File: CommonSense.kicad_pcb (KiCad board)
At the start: 2 copper layers, 34 x 24 mm, 31 parts, among them J1 Conn_02x04_Counter_Clockwise, U1 NRF52810-QFAA-R7, U2 SHT41-AD1B-R2, Y1 ECS-.327-12.5-12R-TR, Y2 ABM11W-32.0000MHZ-7-D1X-T3

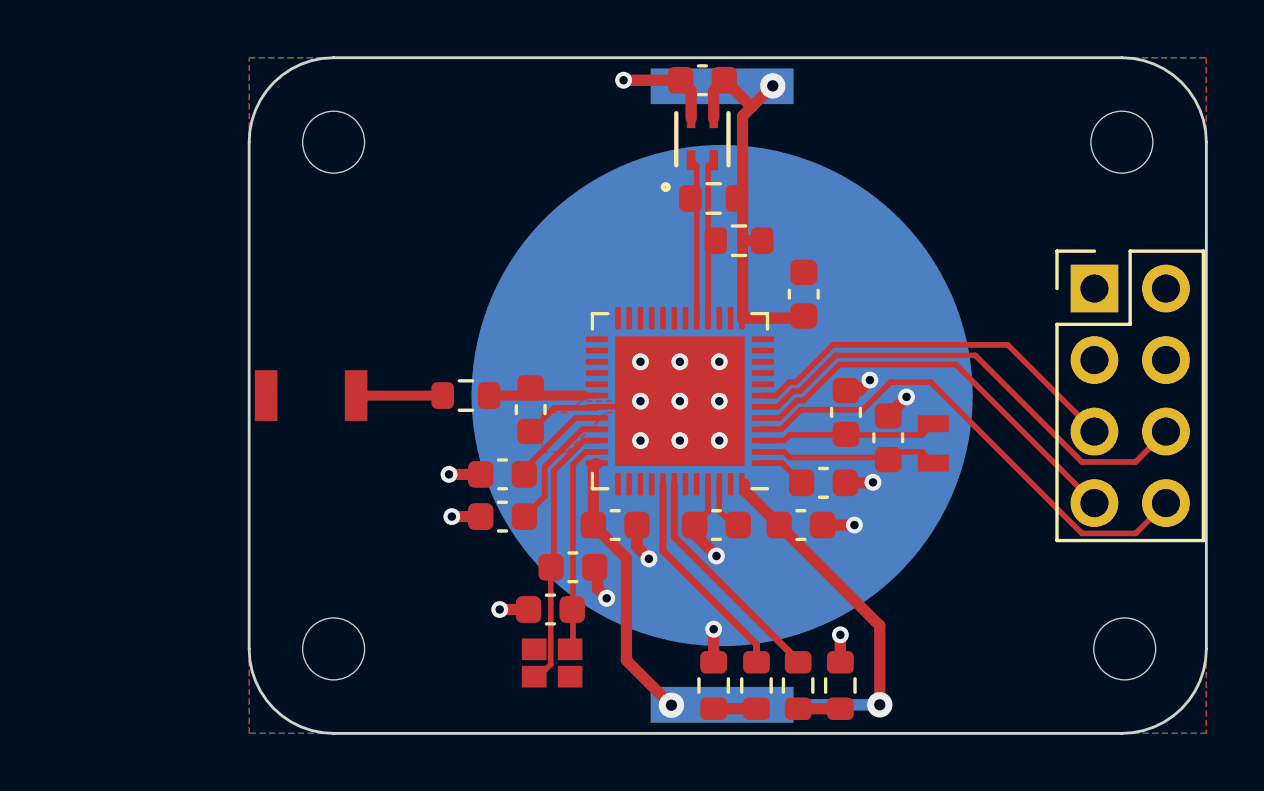
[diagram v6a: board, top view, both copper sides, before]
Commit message: Finish routing ADC in IO pins
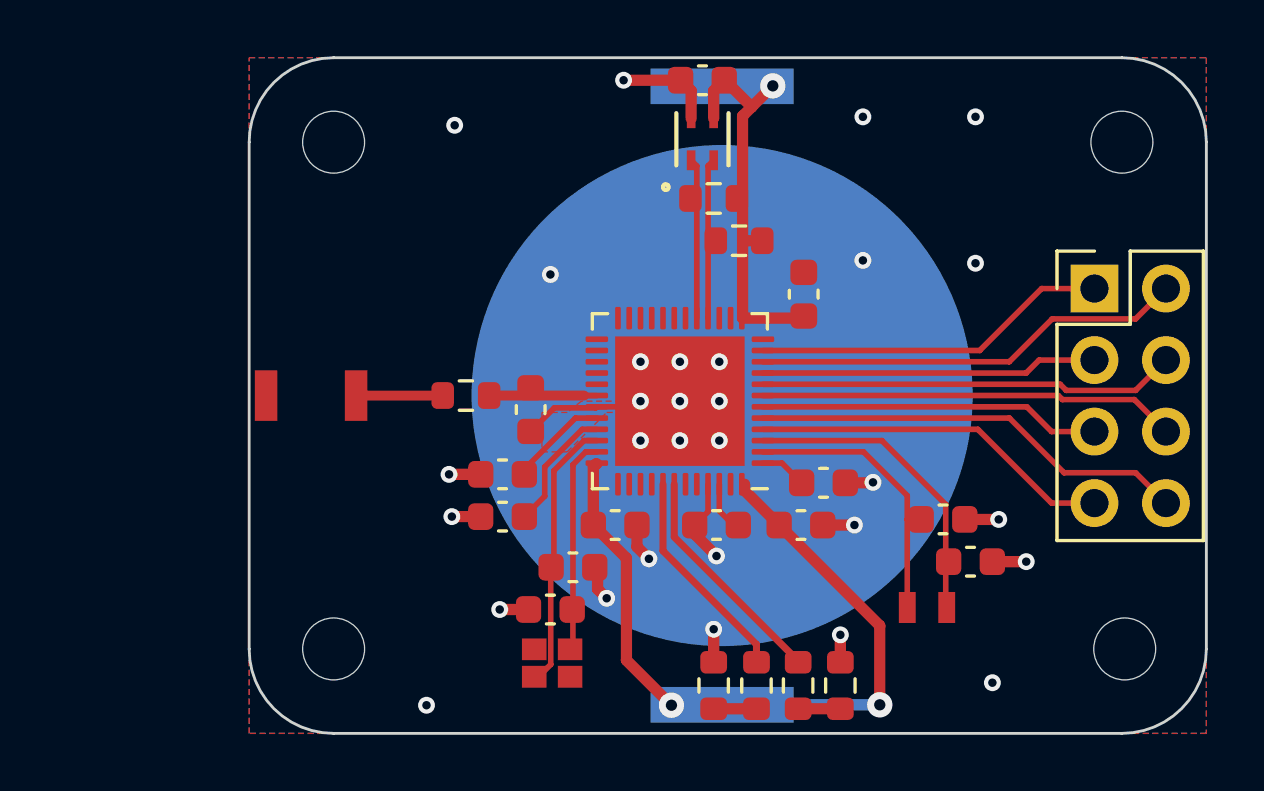
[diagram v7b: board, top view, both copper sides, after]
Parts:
- moved C2 6.90 mm to (161.6, 73.9), turned to 0 degrees
- moved Y1 5.83 mm to (160.1, 75.5), turned to 180 degrees
- moved C1 3.49 mm to (160.6, 72.4), turned to 0 degrees
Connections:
- J1 pad 5: /AIN3 -> /AIN2
- J1 pad 6: /AIN2 -> /AIN3
- J1 pad 7: /AIN1 -> /AIN0
- J1 pad 8: /AIN0 -> /AIN1
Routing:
- net /P0.08: track 0.00 -> 15.4 mm
- net /P0.06: track 0.00 -> 14.9 mm
- net /P0.09: track 0.00 -> 12.7 mm
- net /P0.07: track 0.00 -> 12.0 mm
- net /AIN2: track 17.1 -> 12.1 mm
- net /AIN0: track 17.7 -> 12.9 mm
- net /XL2: track 6.32 -> 11.1 mm
- net /XL1: track 6.44 -> 10.2 mm
- net /AIN3: track 13.8 -> 14.9 mm
- net /AIN1: track 14.6 -> 15.6 mm
- net GND: track 22.9 -> 23.4 mm, vias 22 -> 30

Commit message: Add forgotten ground vias
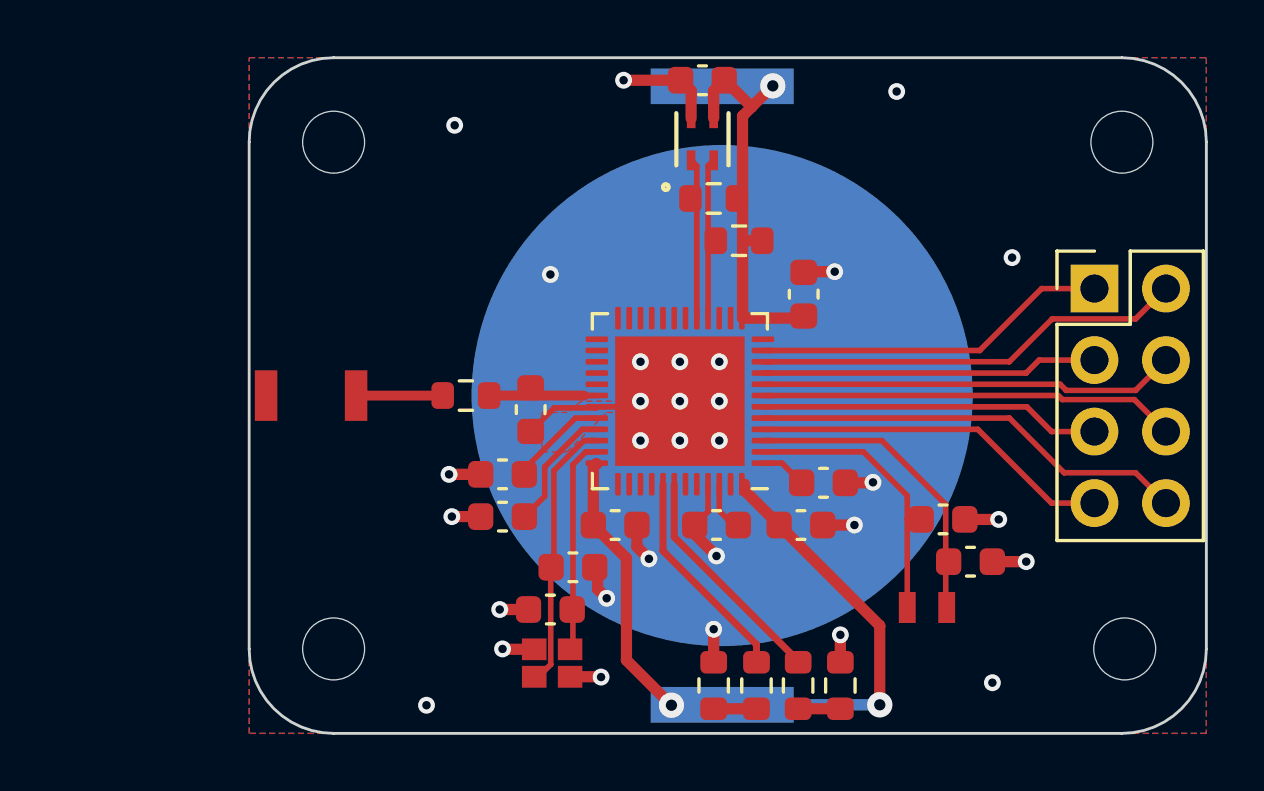
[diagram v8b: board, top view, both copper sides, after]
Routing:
- net GND: track 23.4 -> 26.8 mm, vias 30 -> 31
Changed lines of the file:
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@@
   (segment (start 158.15864 71.08272) (end 158.14136 71.1) (width 0.4) (layer "F.Cu") (net 3))
   (segment (start 152.3 71.15) (end 152.3 72.125) (width 0.2) (layer "F.Cu") (net 3))
+  (segment (start 156.8 63.6) (end 155.725 63.6) (width 0.4) (layer "F.Cu") (net 3))
+  (segment (start 148.487 77.987) (end 148.5 78) (width 0.4) (layer "F.Cu") (net 3))
   (segment (start 149.7 68.4) (end 149.9 68.2) (width 0.2) (layer "F.Cu") (net 3))
   (segment (start 151.69995 57.17495) (end 151.325 56.8) (width 0.4) (layer "F.Cu") (net 3))
   (segment (start 149.775 73.375) (end 150.2 73.8) (width 0.4) (layer "F.Cu") (net 3))
+  (segment (start 155.725 63.6) (end 155.7 63.625) (width 0.4) (layer "F.Cu") (net 3))
   (segment (start 151.325 56.8) (end 149.3 56.8) (width 0.4) (layer "F.Cu") (net 3))
   (segment (start 152.3 72.125) (end 151.825 72.6) (width 0.2) (layer "F.Cu") (net 3))
   (segment (start 151.825 72.925) (end 152.6 73.7) (width 0.4) (layer "F.Cu") (net 3))
   (segment (start 145.925 75.6) (end 144.9 75.6) (width 0.4) (layer "F.Cu") (net 3))
+  (segment (start 145.013 77.013) (end 145 77) (width 0.4) (layer "F.Cu") (net 3))
   (segment (start 148.375 74.1) (end 148.375 74.875) (width 0.4) (layer "F.Cu") (net 3))
   (segment (start 157 77.475) (end 157 76.5) (width 0.4) (layer "F.Cu") (net 3))
@@
   (segment (start 148.35 68.4) (end 149.7 68.4) (width 0.2) (layer "F.Cu") (net 3))
   (segment (start 162.39755 73.900001) (end 163.60245 73.899999) (width 0.4) (layer "F.Cu") (net 3))
+  (segment (start 146.1255 77.013) (end 145.013 77.013) (width 0.4) (layer "F.Cu") (net 3))
+  (segment (start 147.3995 77.987) (end 148.487 77.987) (width 0.4) (layer "F.Cu") (net 3))
   (via (at 157.5 72.6) (size 0.6) (drill 0.3) (layers "F.Cu" "B.Cu") (net 3))
   (via (at 151.3 69.6) (size 0.6) (drill 0.3) (layers "F.Cu" "B.Cu") (net 3))
@@
   (via (at 162.4 78.2) (size 0.6) (drill 0.3) (layers "F.Cu" "B.Cu") (net 3))
   (via (at 158.15864 71.08272) (size 0.6) (drill 0.3) (layers "F.Cu" "B.Cu") (net 3))
-  (via (at 161.8 58.1) (size 0.6) (drill 0.3) (layers "F.Cu" "B.Cu") (net 3))
+  (via (at 163.1 63.1) (size 0.6) (drill 0.3) (layers "F.Cu" "B.Cu") (net 3))
   (via (at 144.9 75.6) (size 0.6) (drill 0.3) (layers "F.Cu" "B.Cu") (net 3))
   (via (at 157 76.5) (size 0.6) (drill 0.3) (layers "F.Cu" "B.Cu") (net 3))
+  (via (at 148.5 78) (size 0.6) (drill 0.3) (layers "F.Cu" "B.Cu") (net 3))
   (via (at 148.7 75.2) (size 0.6) (drill 0.3) (layers "F.Cu" "B.Cu") (net 3))
   (via (at 149.9 68.2) (size 0.6) (drill 0.3) (layers "F.Cu" "B.Cu") (net 3))
   (via (at 162.624999 72.400001) (size 0.6) (drill 0.3) (layers "F.Cu" "B.Cu") (net 3))
-  (via (at 161.8 63.3) (size 0.6) (drill 0.3) (layers "F.Cu" "B.Cu") (net 3))
   (via (at 152.5 76.3) (size 0.6) (drill 0.3) (layers "F.Cu" "B.Cu") (net 3))
   (via (at 149.3 56.8) (size 0.6) (drill 0.3) (layers "F.Cu" "B.Cu") (net 3))
@@
   (via (at 149.9 69.6) (size 0.6) (drill 0.3) (layers "F.Cu" "B.Cu") (net 3))
   (via (at 146.7 63.7) (size 0.6) (drill 0.3) (layers "F.Cu" "B.Cu") (net 3))
-  (via (at 157.8 63.2) (size 0.6) (drill 0.3) (layers "F.Cu" "B.Cu") (net 3))
+  (via (at 156.8 63.6) (size 0.6) (drill 0.3) (layers "F.Cu" "B.Cu") (net 3))
   (via (at 150.2 73.8) (size 0.6) (drill 0.3) (layers "F.Cu" "B.Cu") (net 3))
   (via (at 143.3 58.4) (size 0.6) (drill 0.3) (layers "F.Cu" "B.Cu") (net 3))
@@
   (via (at 151.3 68.2) (size 0.6) (drill 0.3) (layers "F.Cu" "B.Cu") (net 3))
   (via (at 152.6 73.7) (size 0.6) (drill 0.3) (layers "F.Cu" "B.Cu") (net 3))
-  (via (at 157.8 58.1) (size 0.6) (drill 0.3) (layers "F.Cu" "B.Cu") (net 3))
+  (via (at 159 57.2) (size 0.6) (drill 0.3) (layers "F.Cu" "B.Cu") (net 3))
+  (via (at 145 77) (size 0.6) (drill 0.3) (layers "F.Cu" "B.Cu") (net 3))
   (via (at 143.2 72.3) (size 0.6) (drill 0.3) (layers "F.Cu" "B.Cu") (net 3))
   (via (at 151.3 66.8) (size 0.6) (drill 0.3) (layers "F.Cu" "B.Cu") (net 3))
